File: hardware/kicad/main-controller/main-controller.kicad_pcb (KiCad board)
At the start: 2 copper layers, 24 parts, among them J1 12V FUSED, J10 CELL XH, J11 KINDLE CHARGE, J12 HX711 digital, J13 BUS3, J14 BUS4, J3 BUCK_ESP Mini560 5V, J4 BUCK_USB Mini560 5V, J5 DevKit J1 left, J6 DevKit J3 right, J7 BUS1, J8 BUS2, J9 HX711 analog, SW1 MAIN 10A DC

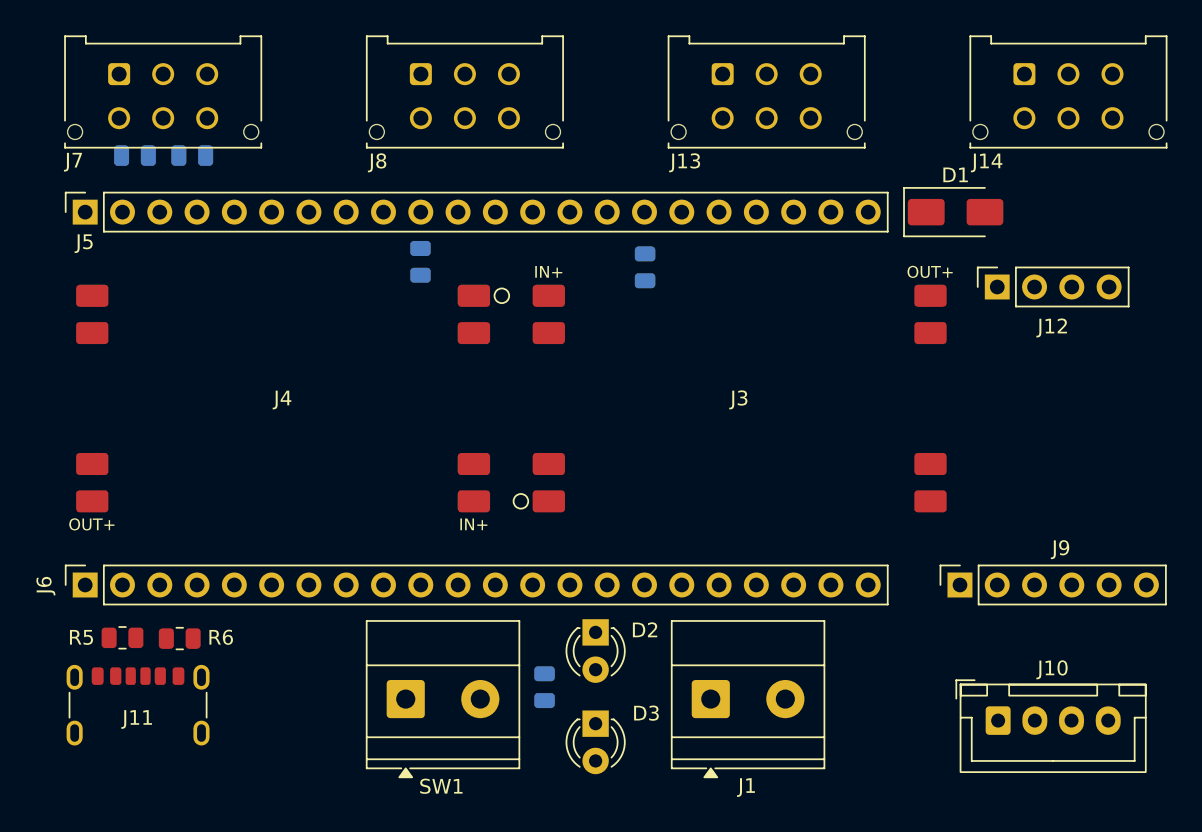
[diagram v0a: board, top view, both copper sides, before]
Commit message: Lock in both PCBs for fab and sync hardware, firmware pins, and procurement.
4-pump and main-controller KiCad layouts are ordered; motherboard GPIO map, CAD refs, bench logs, and AliExpress/OSH Park procurement notes are brought current so assembly can proceed when boards arrive.

Co-authored-by: Cursor <cursoragent@cursor.com>
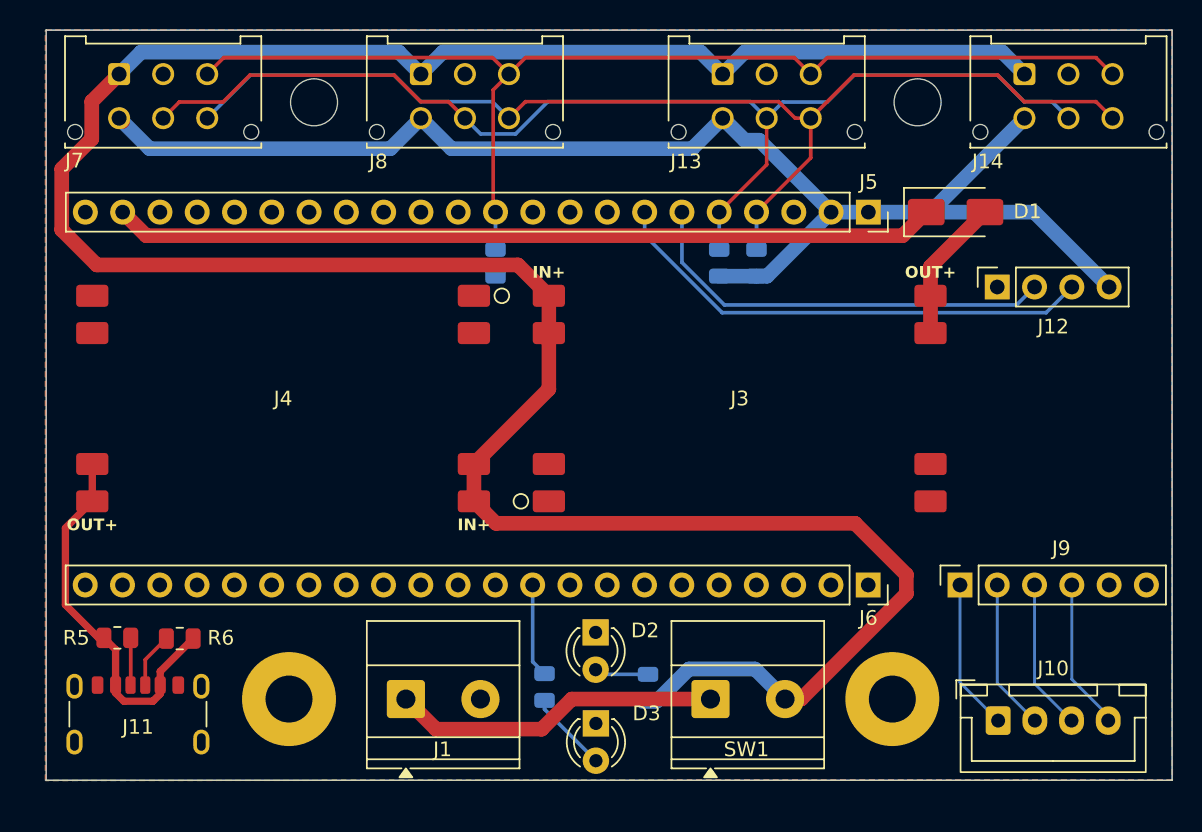
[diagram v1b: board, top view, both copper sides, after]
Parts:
- added H1: MountingHole, MountingHole:MountingHole_3.2mm_M3, F.Cu at (123.2, 59.0)
- added H2: MountingHole, MountingHole:MountingHole_3.2mm_M3, F.Cu at (164.3, 59.0)
- added H3: MountingHole_Pad, MountingHole:MountingHole_3.2mm_M3_Pad, F.Cu at (121.5, 99.7)
- added H4: MountingHole_Pad, MountingHole:MountingHole_3.2mm_M3_Pad, F.Cu at (162.6, 99.7)
- moved J5 53.4 mm to (161.0, 66.5), turned to -90 degrees
- moved J6 53.3 mm to (160.9, 91.9), turned to -90 degrees
- moved R2 40.5 mm to (150.8, 70.0), turned to 90 degrees
- moved R3 39.1 mm to (153.3, 70.0), turned to 90 degrees
- moved R7 29.4 mm to (138.9, 98.8)
- moved J1 20.8 mm to (129.5, 99.7)
- moved SW1 20.8 mm to (150.2, 99.7)
- moved R1 7.05 mm to (145.9, 98.9)
- moved R4 5.11 mm to (135.6, 70.0)
- moved J11 0.61 mm to (111.2, 101.8)
- moved R5 0.35 mm to (109.8, 95.5)
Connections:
- J5 pad 10: /PUMP_BUS_ENABLE -> unconnected-(J5-Pin_10-Pad10)
- J5 pad 11: unconnected-(J5-Pin_11-Pad11) -> /PUMP_BUS_ENABLE
- J5 pad 12: /HX711_DT -> unconnected-(J5-Pin_12-Pad12)
- J5 pad 15: /HX711_SCK -> unconnected-(J5-Pin_15-Pad15)
- J5 pad 16: /LED_STATUS -> unconnected-(J5-Pin_16-Pad16)
- J5 pad 17: /SDA -> unconnected-(J5-Pin_17-Pad17)
- J5 pad 18: /SCL -> unconnected-(J5-Pin_18-Pad18)
- J5 pad 4: unconnected-(J5-Pin_4-Pad4) -> /SCL
- J5 pad 5: unconnected-(J5-Pin_5-Pad5) -> /SDA
- J5 pad 6: unconnected-(J5-Pin_6-Pad6) -> /HX711_DT
- J5 pad 7: unconnected-(J5-Pin_7-Pad7) -> /HX711_SCK
- J6 pad 10: unconnected-(J6-Pin_10-Pad10) -> /LED_STATUS
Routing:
- net /+12V_SW: track 0.00 -> 183.9 mm
- net +3V3: track 0.00 -> 94.4 mm
- net /SDA: track 0.00 -> 78.8 mm
- net /SCL: track 0.00 -> 77.9 mm
- net /PUMP_BUS_ENABLE: track 0.00 -> 76.9 mm
- net /+5V_DEV: track 0.00 -> 56.1 mm
- net /HX711_SCK: track 0.00 -> 33.6 mm
- net /HX711_DT: track 0.00 -> 29.2 mm
- net /+5V_USB: track 0.00 -> 26.2 mm
- net /+12V: track 0.00 -> 22.4 mm
- net /E+: track 0.00 -> 10.3 mm
- net /E-: track 0.00 -> 10.3 mm
- net /A-: track 0.00 -> 10.3 mm
- net /A+: track 0.00 -> 10.3 mm
- net /+5V_ESP: track 0.00 -> 9.78 mm
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- added copper zone on B.Cu, net GND
- added copper zone on F.Cu, net GND
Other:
- board outline added: 76.7 x 51.1 mm
- board text added: "Rumtime Main Board v1.0 Chris Lawson"
- board text added: "try { pourRum(); } catch RumtimeException { pourRumHarder(); }"
